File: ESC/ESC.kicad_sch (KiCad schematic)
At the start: 19 parts, among them J4 swd, J5 input, SW1 Boot0, SW2 NRST, U1 STM32F411RETx, Y1 16Mhz?

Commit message: finished a mockup of the pcb layout
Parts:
- J4: footprint (none) -> Connector_PinHeader_2.54mm:PinHeader_1x04_P2.54mm_Vertical
- J5: footprint (none) -> Connector_PinHeader_2.54mm:PinHeader_1x03_P2.54mm_Vertical
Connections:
- net +3.3V: now also SW1.3 (C)
- net +3.3VA: no longer SW1.3 (C)
- net GND: now also C1.2, C10.2, C2.2, C3.2, C4.2, C5.2, C6.2, C7.2
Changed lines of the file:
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@@
   (junction (at 27.94 23.495) (diameter 0) (color 0 0 0 0)
   )
+  (junction (at 81.28 35.56) (diameter 0) (color 0 0 0 0)
+  )
   (junction (at 31.75 90.17) (diameter 0) (color 0 0 0 0)
   )
@@
   (junction (at 27.94 35.56) (diameter 0) (color 0 0 0 0)
   )
+  (junction (at 41.91 35.56) (diameter 0) (color 0 0 0 0)
+  )
   (junction (at 16.51 90.17) (diameter 0) (color 0 0 0 0)
+  )
+  (junction (at 41.91 23.495) (diameter 0) (color 0 0 0 0)
   )
   (junction (at 46.355 23.495) (diameter 0) (color 0 0 0 0)
@@
     (stroke (width 0) (type default))
   )
+  (wire (pts (xy 41.91 23.495) (xy 46.355 23.495))
+    (stroke (width 0) (type default))
+  )
   (wire (pts (xy 106.045 41.275) (xy 106.045 43.815))
     (stroke (width 0) (type default))
@@
     (stroke (width 0) (type default))
   )
-  (wire (pts (xy 36.83 23.495) (xy 46.355 23.495))
+  (wire (pts (xy 36.83 23.495) (xy 41.91 23.495))
     (stroke (width 0) (type default))
   )
@@
     (stroke (width 0) (type default))
   )
+  (wire (pts (xy 41.91 35.56) (xy 46.355 35.56))
+    (stroke (width 0) (type default))
+  )
   (wire (pts (xy 55.245 35.56) (xy 64.135 35.56))
     (stroke (width 0) (type default))
@@
     (stroke (width 0) (type default))
   )
-  (wire (pts (xy 36.83 35.56) (xy 46.355 35.56))
+  (wire (pts (xy 36.83 35.56) (xy 41.91 35.56))
     (stroke (width 0) (type default))
   )
@@
     (stroke (width 0) (type default))
   )
+  (wire (pts (xy 81.28 35.56) (xy 85.725 35.56))
+    (stroke (width 0) (type default))
+  )
   (wire (pts (xy 116.205 59.055) (xy 165.735 59.055))
     (stroke (width 0) (type default))
@@
     (stroke (width 0) (type default))
   )
+  (wire (pts (xy 41.91 36.195) (xy 41.91 35.56))
+    (stroke (width 0) (type default))
+  )
   (wire (pts (xy 16.51 93.345) (xy 16.51 90.17))
     (stroke (width 0) (type default))
@@
     (stroke (width 0) (type default))
   )
-  (wire (pts (xy 76.835 35.56) (xy 85.725 35.56))
+  (wire (pts (xy 76.835 35.56) (xy 81.28 35.56))
     (stroke (width 0) (type default))
   )
@@
   )
   (text_box "Added one decoupling capacitor for every power pin and an extra bulk decoupling capacitor for both digital and analog power\n"
-    (at 14.605 36.83 0) (size 25.4 15.24)
+    (at -10.16 22.86 0) (size 25.4 15.24)
     (stroke (width 0) (type default))
     (fill (type none))
@@
     )
   )
-  (symbol (lib_id "power:+3.3VA") (at 44.45 51.435 0) (unit 1)
-    (in_bom yes) (on_board yes) (dnp no) (fields_autoplaced)
-    (property "Reference" "#PWR07" (at 44.45 55.245 0)
-      (effects (font (size 1.27 1.27)) hide)
-    )
-    (property "Value" "+3.3VA" (at 44.45 46.99 0)
+  (symbol (lib_id "power:GND") (at 41.91 36.195 0) (unit 1)
+    (in_bom yes) (on_board yes) (dnp no) (fields_autoplaced)
+    (property "Reference" "#PWR016" (at 41.91 42.545 0)
+      (effects (font (size 1.27 1.27)) hide)
+    )
+    (property "Value" "GND" (at 41.91 41.275 0)
       (effects (font (size 1.27 1.27)))
     )
-    (property "Footprint" "" (at 44.45 51.435 0)
-      (effects (font (size 1.27 1.27)) hide)
-    )
-    (property "Datasheet" "" (at 44.45 51.435 0)
-      (effects (font (size 1.27 1.27)) hide)
-    )
-    (pin "1")
-    (instances
-      (project "ESC"
-        (path "/88e9b63e-ca06-4d41-87b7-50146fa458bf"
-          (reference "#PWR07") (unit 1)
-        )
-      )
-    )
-  )
-  (symbol (lib_id "power:+3.3V") (at 36.83 23.495 0) (unit 1)
-    (in_bom yes) (on_board yes) (dnp no) (fields_autoplaced)
-    (property "Reference" "#PWR01" (at 36.83 27.305 0)
-      (effects (font (size 1.27 1.27)) hide)
-    )
-    (property "Value" "+3.3V" (at 36.83 18.415 0)
+    (property "Footprint" "" (at 41.91 36.195 0)
+      (effects (font (size 1.27 1.27)) hide)
+    )
+    (property "Datasheet" "" (at 41.91 36.195 0)
+      (effects (font (size 1.27 1.27)) hide)
+    )
+    (pin "1")
+    (instances
+      (project "ESC"
+        (path "/88e9b63e-ca06-4d41-87b7-50146fa458bf"
+          (reference "#PWR016") (unit 1)
+        )
+      )
+    )
+  )
+  (symbol (lib_id "power:+3.3V") (at 41.91 23.495 0) (unit 1)
+    (in_bom yes) (on_board yes) (dnp no) (fields_autoplaced)
+    (property "Reference" "#PWR01" (at 41.91 27.305 0)
+      (effects (font (size 1.27 1.27)) hide)
+    )
+    (property "Value" "+3.3V" (at 41.91 18.415 0)
       (effects (font (size 1.27 1.27)))
     )
-    (property "Footprint" "" (at 36.83 23.495 0)
-      (effects (font (size 1.27 1.27)) hide)
-    )
-    (property "Datasheet" "" (at 36.83 23.495 0)
+    (property "Footprint" "" (at 41.91 23.495 0)
+      (effects (font (size 1.27 1.27)) hide)
+    )
+    (property "Datasheet" "" (at 41.91 23.495 0)
       (effects (font (size 1.27 1.27)) hide)
     )
@@
       (effects (font (size 1.27 1.27)) (justify right))
     )
-    (property "Footprint" "" (at 176.53 88.9 0)
+    (property "Footprint" "Connector_PinHeader_2.54mm:PinHeader_1x04_P2.54mm_Vertical" (at 176.53 88.9 0)
       (effects (font (size 1.27 1.27)) hide)
     )
@@
       (effects (font (size 1.27 1.27)) (justify right))
     )
-    (property "Footprint" "" (at 176.53 106.68 0)
+    (property "Footprint" "Connector_PinHeader_2.54mm:PinHeader_1x03_P2.54mm_Vertical" (at 176.53 106.68 0)
       (effects (font (size 1.27 1.27)) hide)
     )
@@
     )
   )
+  (symbol (lib_id "power:GND") (at 81.28 35.56 0) (unit 1)
+    (in_bom yes) (on_board yes) (dnp no) (fields_autoplaced)
+    (property "Reference" "#PWR057" (at 81.28 41.91 0)
+      (effects (font (size 1.27 1.27)) hide)
+    )
+    (property "Value" "GND" (at 81.28 40.64 0)
+      (effects (font (size 1.27 1.27)))
+    )
+    (property "Footprint" "" (at 81.28 35.56 0)
+      (effects (font (size 1.27 1.27)) hide)
+    )
+    (property "Datasheet" "" (at 81.28 35.56 0)
+      (effects (font (size 1.27 1.27)) hide)
+    )
+    (pin "1")
+    (instances
+      (project "ESC"
+        (path "/88e9b63e-ca06-4d41-87b7-50146fa458bf"
+          (reference "#PWR057") (unit 1)
+        )
+      )
+    )
+  )
   (symbol (lib_id "Device:C") (at 46.355 29.21 0) (unit 1)
     (in_bom yes) (on_board yes) (dnp no) (fields_autoplaced)
@@
         )
       )
+    )
+  )
+  (symbol (lib_id "power:+3.3V") (at 44.45 51.435 0) (unit 1)
+    (in_bom yes) (on_board yes) (dnp no) (fields_autoplaced)
+    (property "Reference" "#PWR07" (at 44.45 55.245 0)
+      (effects (font (size 1.27 1.27)) hide)
+    )
+    (property "Value" "+3.3V" (at 44.45 46.99 0)
+      (effects (font (size 1.27 1.27)))
+    )
+    (property "Footprint" "" (at 44.45 51.435 0)
+      (effects (font (size 1.27 1.27)) hide)
+    )
+    (property "Datasheet" "" (at 44.45 51.435 0)
+      (effects (font (size 1.27 1.27)) hide)
+    )
+    (pin "1")
+    (instances
+      (project "ESC"
+        (path "/88e9b63e-ca06-4d41-87b7-50146fa458bf"
+          (reference "#PWR07") (unit 1)
+        )
+      )

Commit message: did some of the routing ofthe PCB
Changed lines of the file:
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@@
+    (effects (font (size 1.27 1.27)) (justify left top))
+  )
+  (text_box "Target PWM frequency = 10kHZ\nDuty cycle range = 10 % - 80 %"
+    (at 216.535 15.24 0) (size 34.925 21.59)
+    (stroke (width 0) (type default))
+    (fill (type none))
     (effects (font (size 1.27 1.27)) (justify left top))
   )

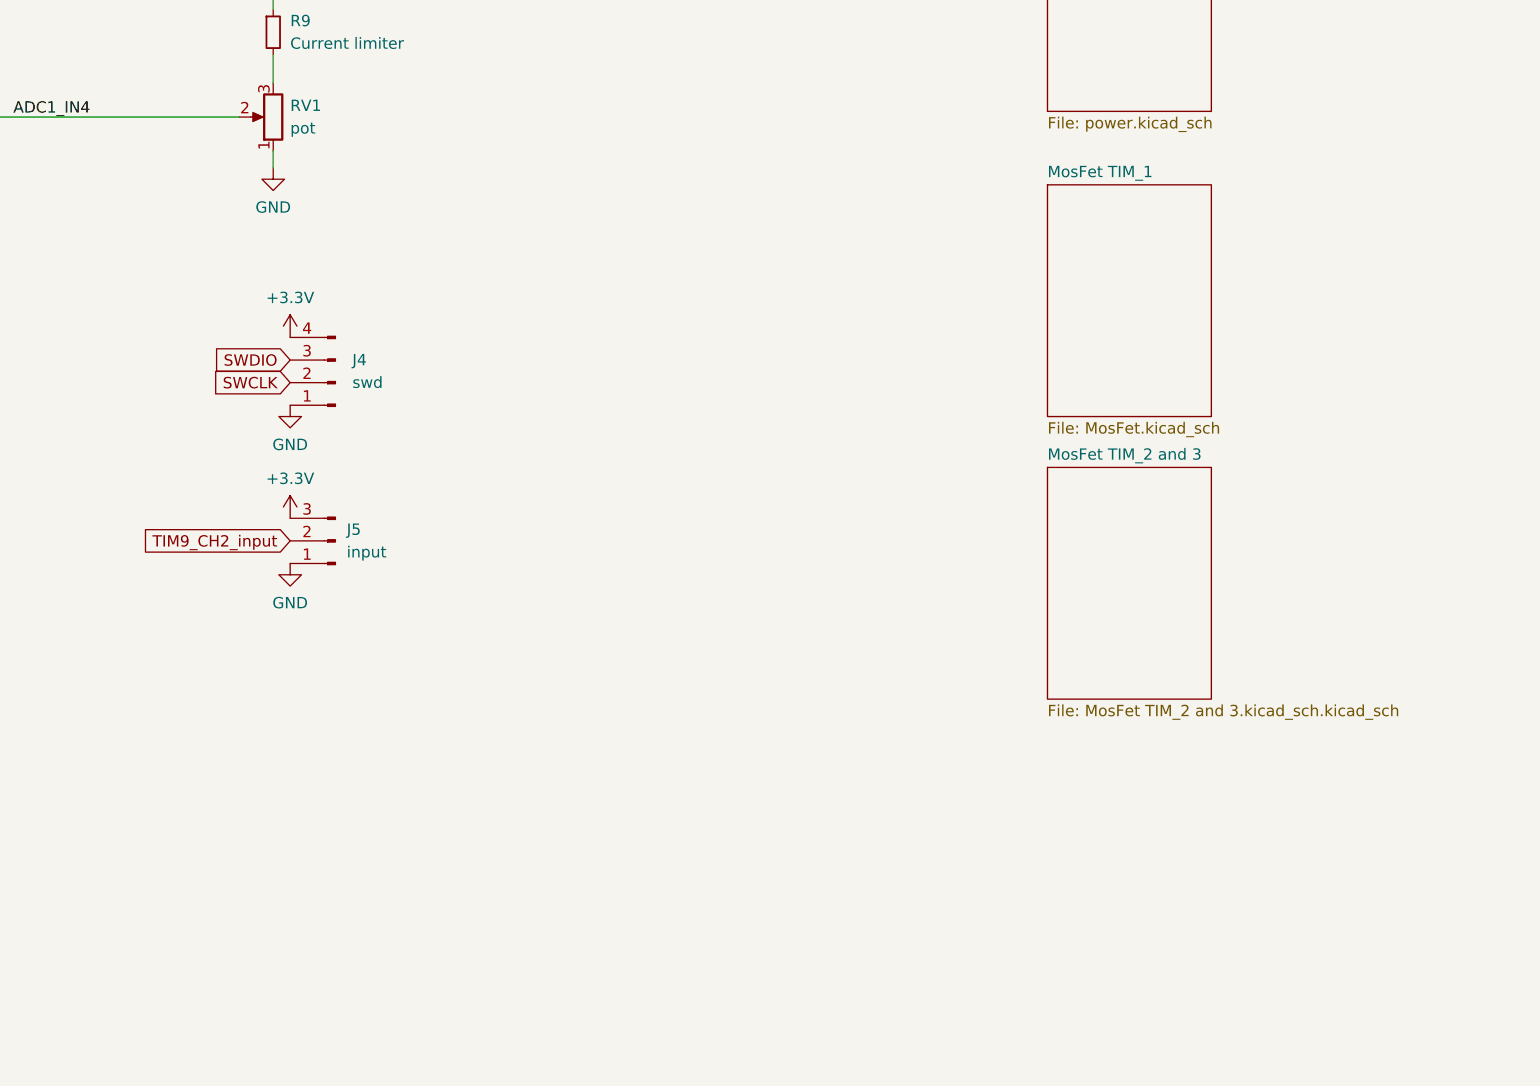
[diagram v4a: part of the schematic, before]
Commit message: changed up the ESC schematic
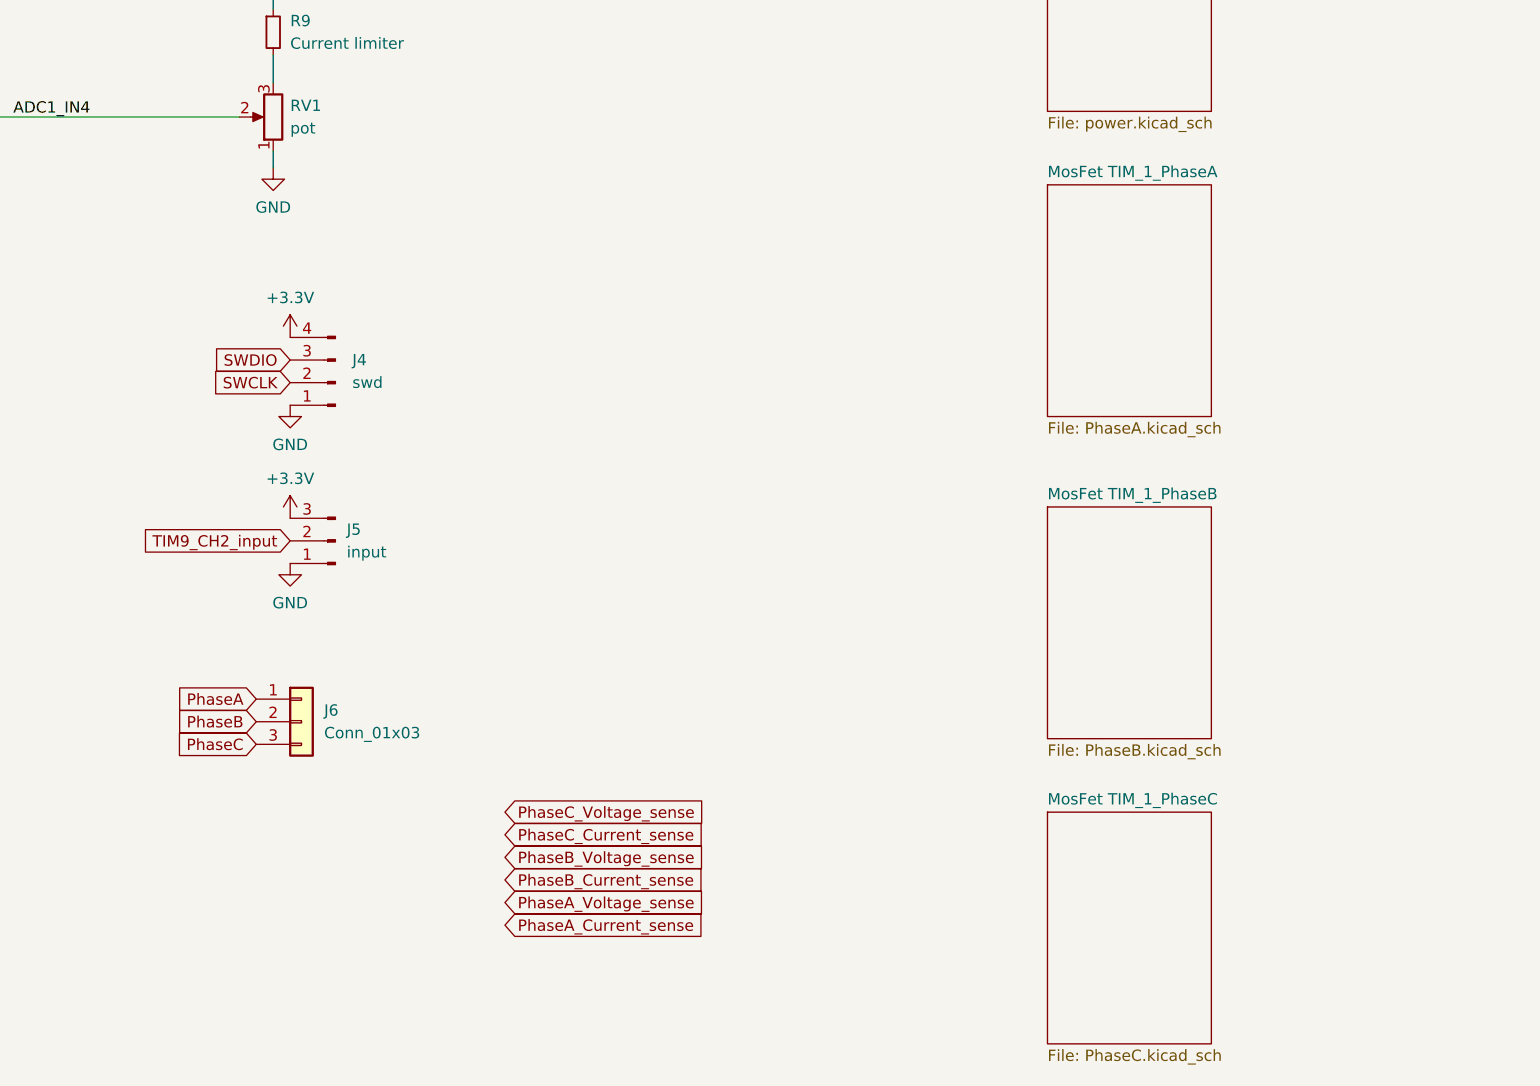
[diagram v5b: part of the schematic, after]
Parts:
- added J6: Conn_01x03, Connector_AMASS:AMASS_MR30PW-FB_1x03_P3.50mm_Horizontal, symbol Connector_Generic:Conn_01x03
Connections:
- new net PhaseA: J6.1 (Pin_1)
- new net PhaseB: J6.2 (Pin_2)
- new net PhaseC: J6.3 (Pin_3)
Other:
- sheet MosFet TIM_1 renamed MosFet TIM_1_PhaseA
- removed sheet MosFet TIM_2 and 3
- added sheet MosFet TIM_1_PhaseB (PhaseB.kicad_sch)
- added sheet MosFet TIM_1_PhaseC (PhaseC.kicad_sch)
- sheet MosFet TIM_1_PhaseA: file MosFet.kicad_sch -> PhaseA.kicad_sch
